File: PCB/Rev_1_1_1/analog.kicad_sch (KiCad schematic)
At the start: 25 parts, among them U2 74HC4051, U3 OPA350, U4 74HC4051

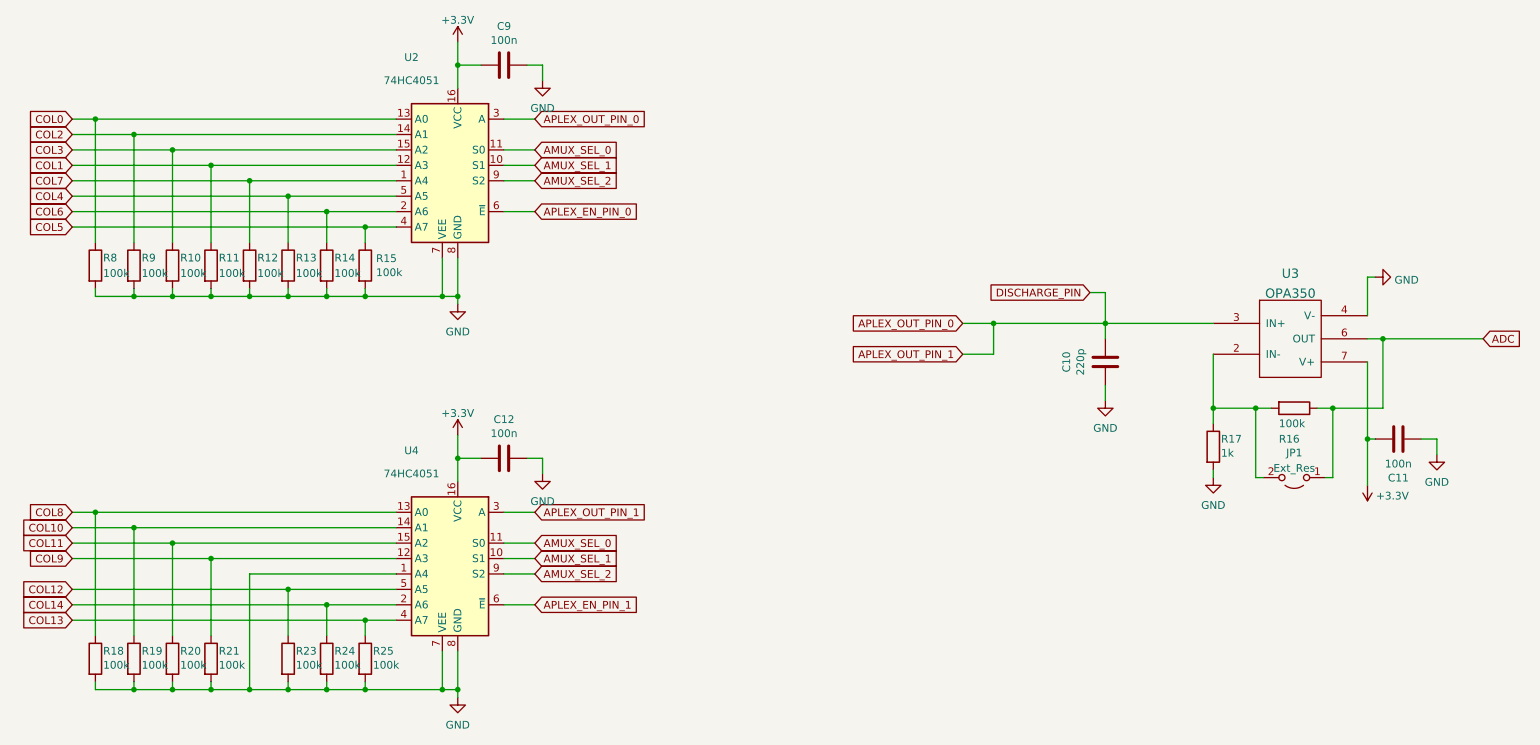
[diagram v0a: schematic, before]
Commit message: Update
Updated the License for the project and relative details.
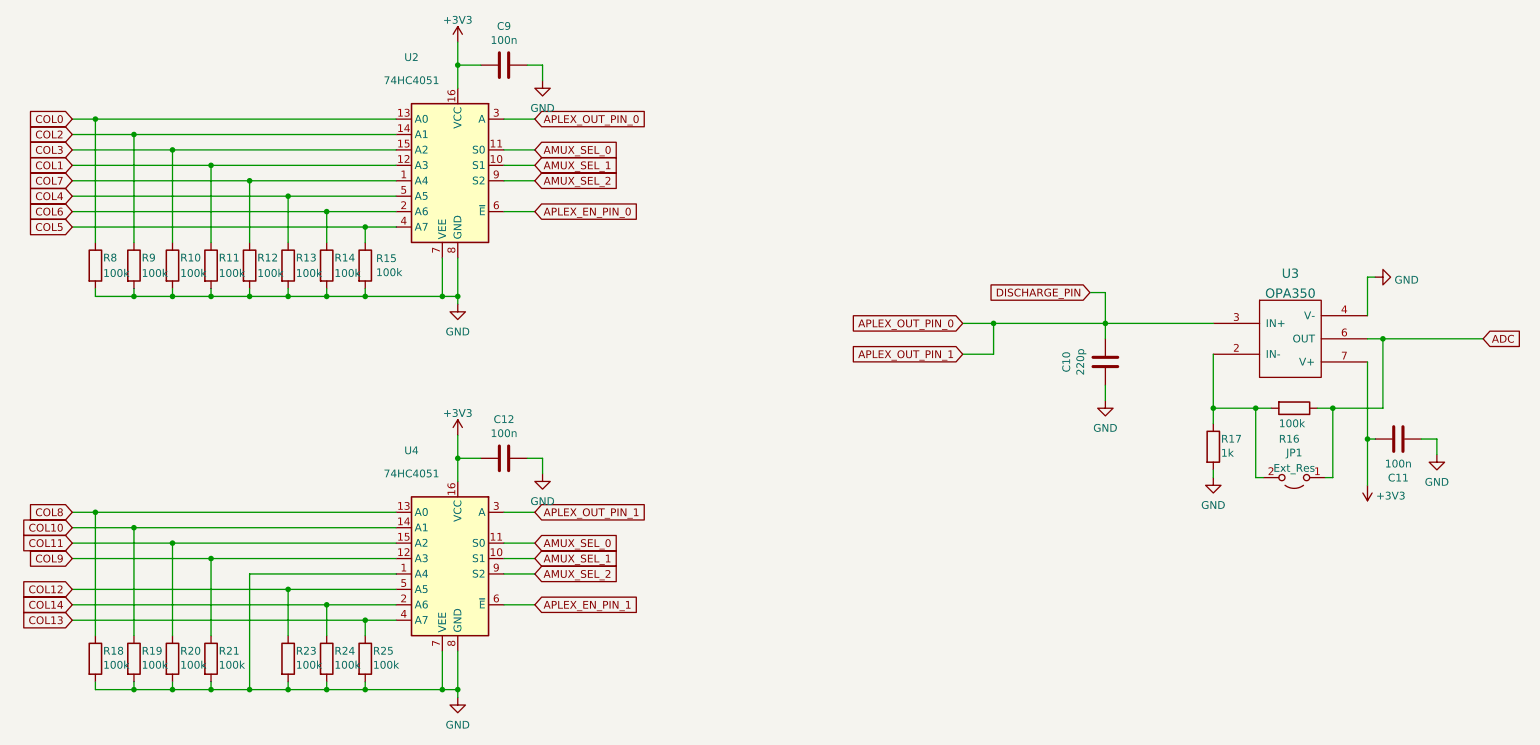
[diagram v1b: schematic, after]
